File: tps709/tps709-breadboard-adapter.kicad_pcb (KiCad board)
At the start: 2 copper layers, 7.7 x 8.6 mm, 4 parts, among them J1 CONN_01X03, U1 TPS709xx

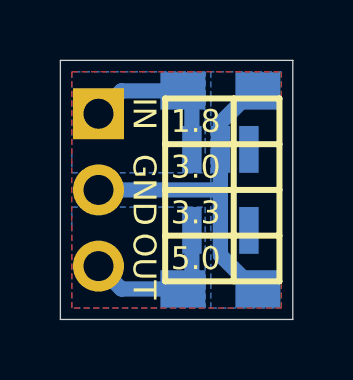
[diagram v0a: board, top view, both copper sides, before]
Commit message: Change tps709 adapter to use 0603 capacitors.
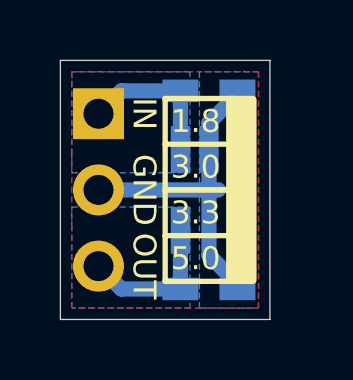
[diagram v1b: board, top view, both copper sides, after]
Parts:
- C1, C2: footprint Capacitors_SMD:C_0805_HandSoldering -> Capacitors_SMD:C_0603_HandSoldering
- moved C1 0.38 mm to (163.4, 105.9)
- moved C2 0.38 mm to (163.4, 112.5)
- moved U1 0.38 mm to (163.4, 109.2)
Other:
- board size 7.7 x 8.6 mm -> 7 x 8.6 mm
